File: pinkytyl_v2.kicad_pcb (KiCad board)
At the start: 2 copper layers, 57 parts, among them J1 AudioJack3, J3 USB_B_Mini, J5 Conn_02x05_Odd_Even, K00 KEYSW, K10 KEYSW, K11 KEYSW, K12 KEYSW, K13 KEYSW, K14 KEYSW, K15 KEYSW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

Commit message: Inc
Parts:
- moved K40 4.13 mm to (183.2, 130.4), turned to 337.5 degrees
- moved K41 3.47 mm to (200.8, 137.6), turned to 337.5 degrees

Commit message: Adds MU version and initial placing
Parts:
- removed D00: D, Diode_SMD:D_SOD-123
- added D0: D, Diode_SMD:D_SOD-123, F.Cu at (94.8, 57.3)
- U1: value ATmega32U4RC-AU -> ATmega32U4-MU; footprint Package_QFP:TQFP-44_10x10mm_P0.8mm -> Package_DFN_QFN:QFN-44-1EP_7x7mm_P0.5mm_EP5.2x5.2mm
- moved D30 317.0 mm to (75.7, 114.4), turned to 270 degrees
- moved D20 307.1 mm to (75.8, 95.3), turned to 270 degrees
- moved D32 269.2 mm to (113.8, 85.0), turned to 270 degrees
- moved D21 261.2 mm to (94.8, 95.3), turned to 270 degrees
- moved D31 256.3 mm to (94.8, 114.2), turned to 270 degrees
- moved D11 253.0 mm to (94.8, 76.5), turned to 270 degrees
- moved C1 250.3 mm to (160.8, 114.8)
- moved R2 246.4 mm to (168.3, 111.3)
- moved R3 245.8 mm to (164.7, 103.9), turned to 180 degrees
- moved R1 242.7 mm to (168.3, 110.1)
- moved Y1 240.0 mm to (163.5, 100.7), turned to 180 degrees
- moved C7 239.6 mm to (167.8, 108.5), turned to 270 degrees
- moved D34 238.5 mm to (151.8, 86.2), turned to 270 degrees
- moved J3 236.5 mm to (190.1, 117.6), turned to 117 degrees
- moved D12 236.2 mm to (113.8, 46.9), turned to 270 degrees
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- renumbered K00 to K0

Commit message: Inc
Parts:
- Y1: value 16MHz -> Crystal_GND24_Small; footprint Crystal:Crystal_SMD_5032-2Pin_5.0x3.2mm -> Crystal:Crystal_SMD_3225-4Pin_3.2x2.5mm
- moved Y1 0.42 mm to (163.8, 100.9), turned to 90 degrees
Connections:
- Y1 pad 2: Net-(C4-Pad1) -> GND
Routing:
- net r2: track 0.00 -> 116.8 mm
- net r1: track 0.00 -> 107.4 mm
- net r3: track 0.00 -> 89.8 mm
- net MOSI: track 0.00 -> 57.0 mm
- net c0: track 0.00 -> 38.0 mm
- net c3: track 0.00 -> 38.0 mm
- net c5: track 0.00 -> 38.0 mm
- net c4: track 0.00 -> 38.0 mm
- net MISO: track 0.00 -> 38.0 mm
- net r0: track 0.00 -> 36.3 mm
- net Net-(D41-Pad2): track 0.00 -> 4.09 mm
- net Net-(D25-Pad2): track 0.00 -> 3.05 mm
- net Net-(D40-Pad2): track 0.00 -> 3.04 mm
- net Net-(D33-Pad2): track 0.00 -> 3.00 mm
- net Net-(D31-Pad2): track 0.00 -> 2.99 mm
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
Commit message: Inc
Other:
- board outline added: 132.2 x 106 mm

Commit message: Inc
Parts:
- moved C3 11.6 mm to (165.2, 115.1), turned to 0 degrees
- moved C5 6.47 mm to (161.6, 102.7), turned to 270 degrees
- moved Y1 5.62 mm to (158.6, 103.0), turned to 180 degrees
- moved C4 4.39 mm to (155.4, 102.7), turned to 90 degrees
- moved D40 4.12 mm to (167.0, 122.8), turned to 315 degrees
- moved D41 3.77 mm to (185.4, 127.2), turned to 342 degrees
- moved D13 3.04 mm to (135.6, 39.2), turned to 225 degrees
- moved D15 3.03 mm to (173.6, 49.5), turned to 225 degrees
- moved D14 2.78 mm to (154.4, 49.3), turned to 225 degrees
- moved C1 2.75 mm to (158.1, 114.5)
- moved D0 2.73 mm to (97.3, 58.4), turned to 225 degrees
- moved D12 2.70 mm to (116.4, 47.8), turned to 225 degrees
- moved D10 2.68 mm to (78.3, 77.4), turned to 225 degrees
- moved J1 2.49 mm to (178.2, 110.9), turned to 297.4 degrees
- moved J5 2.27 mm to (173.9, 99.4)
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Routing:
- net MOSI: track 57.0 -> 172.8 mm, vias 0 -> 2
- net c3: track 38.0 -> 151.2 mm, vias 0 -> 2
- net VCC: track 0.00 -> 105.1 mm, vias 0 -> 13
- net r0: track 36.3 -> 141.2 mm, vias 0 -> 2
- net c0: track 38.0 -> 136.6 mm
- net MISO: track 38.0 -> 132.3 mm, vias 0 -> 1
- net r3: track 89.8 -> 159.7 mm, vias 0 -> 2
- net r2: track 116.8 -> 164.6 mm, vias 0 -> 2
- net c5: track 38.0 -> 82.6 mm, vias 0 -> 2
- net r1: track 107.4 -> 146.2 mm, vias 0 -> 2
- net c4: track 38.0 -> 72.9 mm, vias 0 -> 2
- net d-: track 0.00 -> 24.7 mm
- net d+: track 0.00 -> 24.5 mm
- net serial: track 0.00 -> 22.9 mm, vias 0 -> 2
- net reset: track 0.00 -> 22.2 mm, vias 0 -> 2
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
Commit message: Inc
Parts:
- moved C7 0.77 mm to (168.1, 107.7)
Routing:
- net GND: track 0.00 -> 97.2 mm, vias 0 -> 5
- net Net-(C7-Pad1): track 5.12 -> 6.09 mm
- net c5: track 82.6 -> 83.4 mm
- net c3: track 151.2 -> 151.9 mm
- net VCC: track 105.1 -> 105.7 mm
- net MISO: track 132.3 -> 131.8 mm
- added copper zone on B.Cu, net GND
- added copper zone on F.Cu, net GND

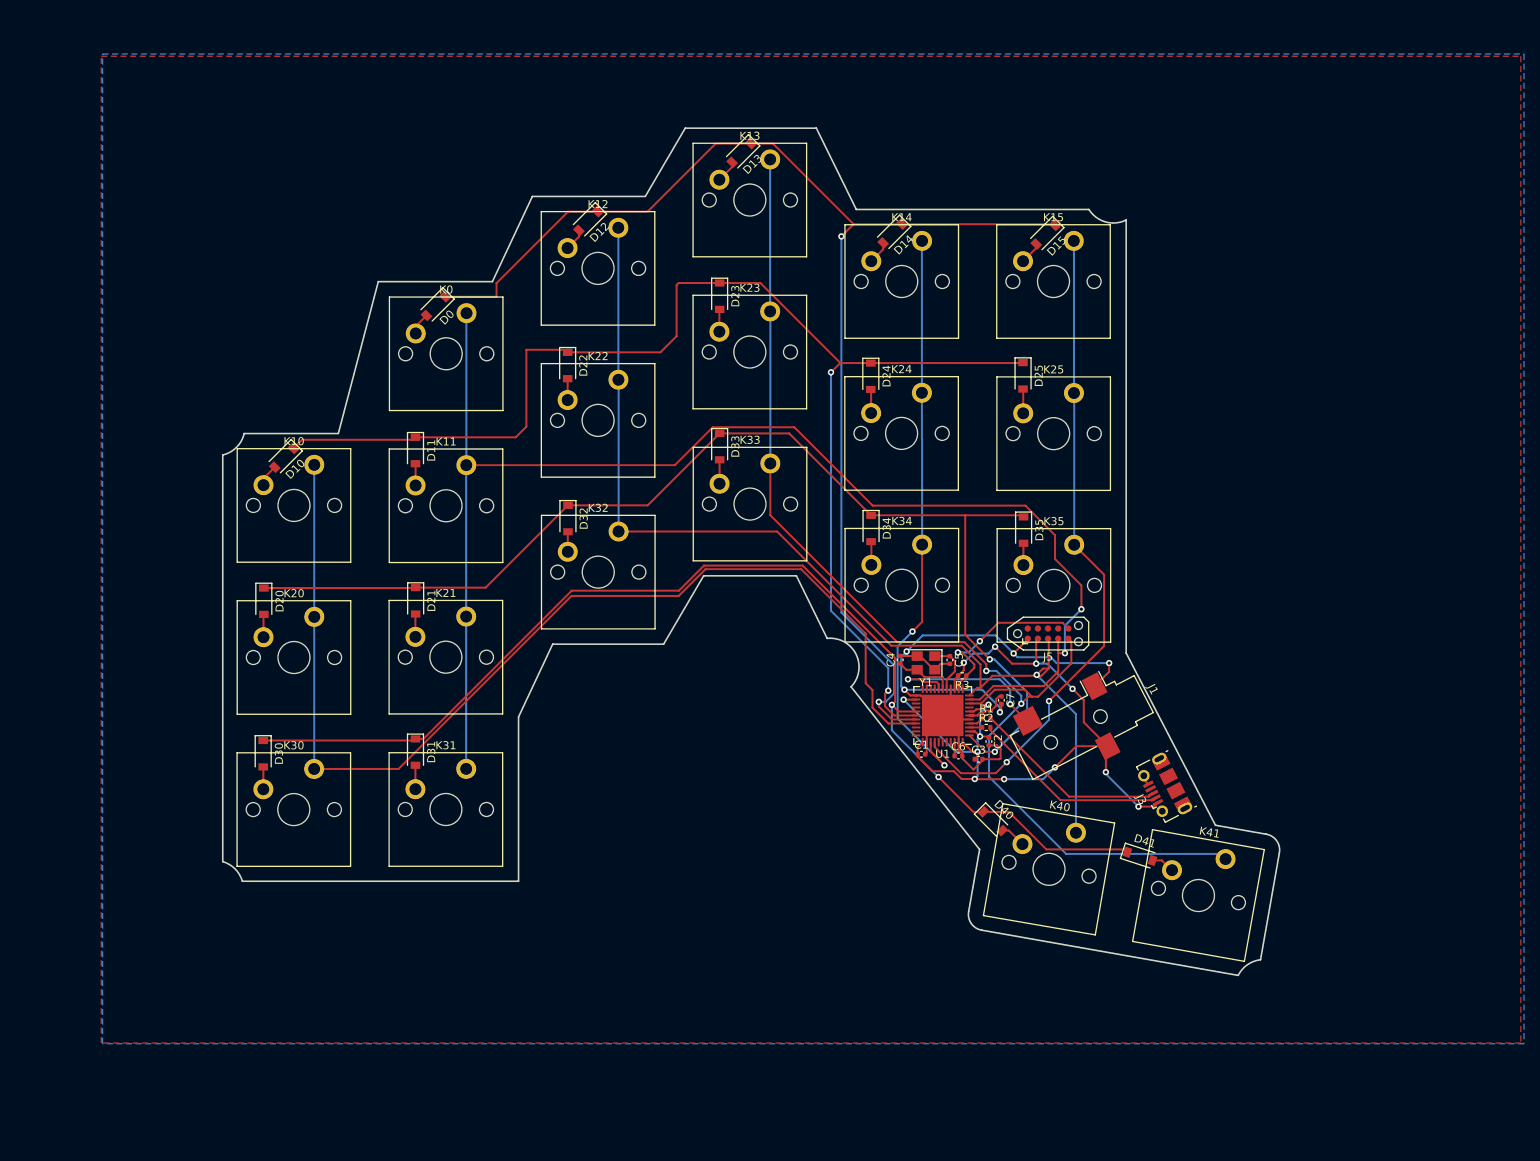
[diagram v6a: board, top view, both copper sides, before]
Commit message: DRC passing and is now double sided
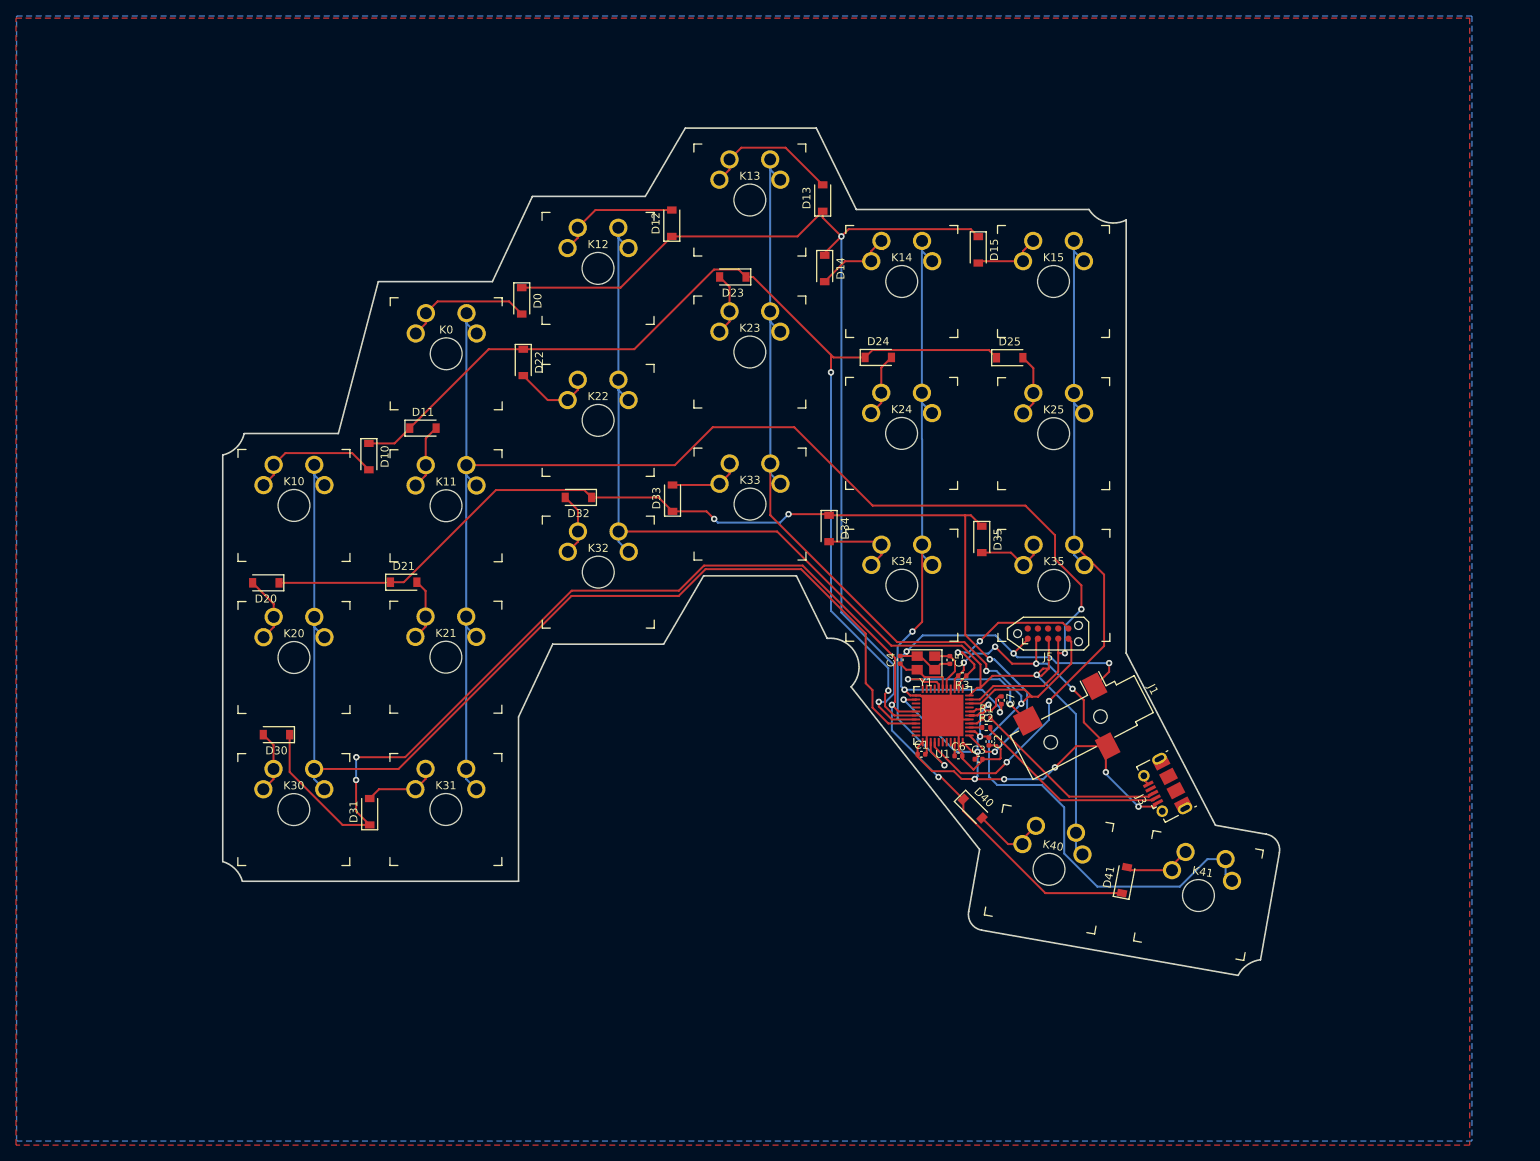
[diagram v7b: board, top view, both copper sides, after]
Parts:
- K0, K10, K11, K12, K13, K14, K15, K20, K21, K22, K23, K24, K25, K30, K31, K32, K33, K34, K35, K40, K41: footprint Switch_Keyboard_Cherry_MX:SW_Cherry_MX_PCB_1.00u -> keyswitches:SW_MX_reversible_minimal
- moved D13 11.6 mm to (145.7, 44.9), turned to 90 degrees
- moved D0 10.8 mm to (108.1, 57.8), turned to 270 degrees
- moved D10 10.6 mm to (89.0, 77.2), turned to 270 degrees
- moved D12 10.5 mm to (126.8, 48.0), turned to 90 degrees
- moved D14 9.54 mm to (146.0, 53.7), turned to 270 degrees
- moved D31 9.41 mm to (89.0, 121.7), turned to 90 degrees
- moved D33 8.73 mm to (126.9, 82.4), turned to 90 degrees
- moved D15 8.63 mm to (165.2, 51.4), turned to 270 degrees
- moved D22 5.56 mm to (108.3, 65.5)
- moved D35 5.36 mm to (165.6, 87.6)
- moved D34 5.25 mm to (146.5, 86.2)
- moved D41 3.56 mm to (183.5, 130.2), turned to 79 degrees
- moved D40 2.97 mm to (164.5, 121.3)
- moved D11 2.95 mm to (95.7, 73.7), turned to 0 degrees
- moved D32 2.95 mm to (115.2, 82.3), turned to 180 degrees
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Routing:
- net r3: track 159.7 -> 135.0 mm
- net r2: track 164.6 -> 144.3 mm
- net c3: track 151.9 -> 171.3 mm
- net r0: track 141.2 -> 159.4 mm, vias 2 -> 4
- net Net-(D13-Pad2): track 2.84 -> 17.8 mm
- net Net-(D10-Pad2): track 2.82 -> 17.3 mm
- net Net-(D0-Pad2): track 2.81 -> 17.2 mm
- net Net-(D12-Pad2): track 2.81 -> 15.8 mm
- net MOSI: track 172.8 -> 185.0 mm
- net r1: track 146.2 -> 134.3 mm, vias 2 -> 4
- net MISO: track 131.8 -> 143.3 mm
- net c4: track 72.9 -> 82.1 mm
- net c0: track 136.6 -> 145.8 mm
- net c5: track 83.4 -> 92.6 mm
- net Net-(D14-Pad2): track 2.91 -> 10.8 mm
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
